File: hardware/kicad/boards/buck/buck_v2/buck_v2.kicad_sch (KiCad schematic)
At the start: 23 parts, among them J1 9V Battery, J2 MCP PWM, J3 Conn_01x02_Socket, Q1 IRF530, SW1 Switch, U1 LM7805, U2 NE555, U3 4N25

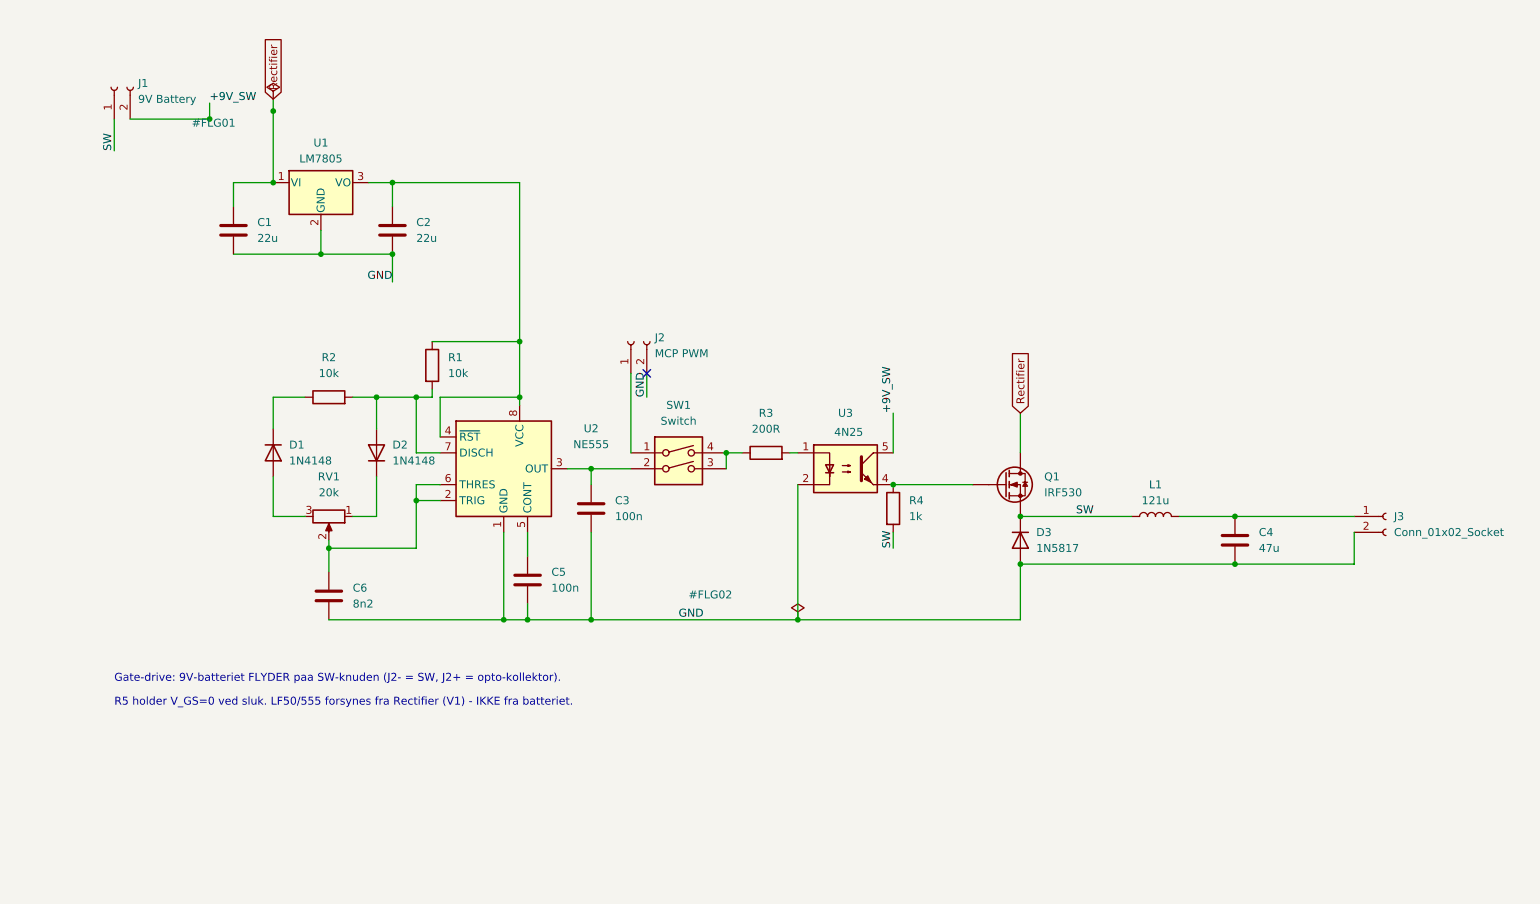
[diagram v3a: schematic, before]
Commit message: Boost v2 med IR2110 gate-driver + boost test-resultater
- boost_v2: integreret IR2110 gate-drive (opto -> IR2110 -> low-side MOSFET),
  generator (build_boost_v2.py), schematic, board og laser/gerber-filer
- buck_v2: patchet til IR2110 high-side drive (patch_buck_v2_ir2110.py)
- boost: opdateret board, gamle produktions-DXF erstattet af boost_v2
- AD3 boost-bringup script (tools/ad3/boost_test.py)
- BOM opdateret med IR2110/CNY17; CNY17- og IRF530-datablade
- rapport: boost maaleresultater (10 kHz, 40%) med figur
- HANDOFF-dokument for buck/boost IR2110-redesign; PCB_RESULTS opdateret
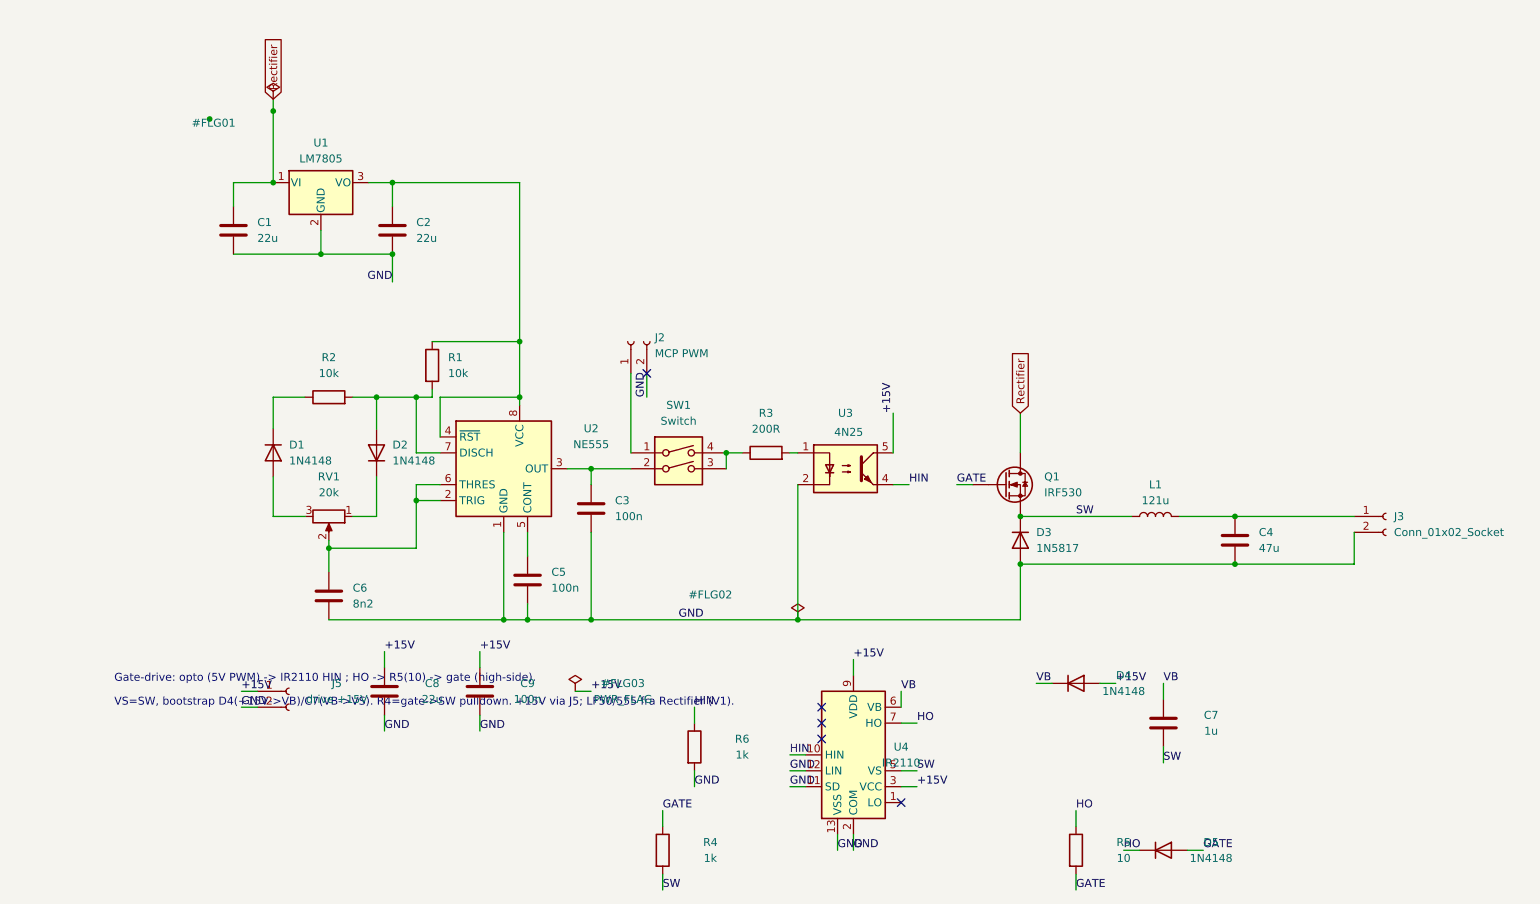
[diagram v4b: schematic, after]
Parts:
- removed J1: 9V Battery, TerminalBlock:TerminalBlock_bornier-2_P5.08mm, symbol Connector:Conn_01x02_Socket
- added C7: 1u, Capacitor_THT:C_Disc_D5.0mm_W2.5mm_P5.00mm, symbol Device:C
- added C8: 22u, Capacitor_THT:CP_Radial_D8.0mm_P3.50mm, symbol Device:C
- added C9: 100n, Capacitor_THT:C_Disc_D5.0mm_W2.5mm_P5.00mm, symbol Device:C
- added D4, D5: 1N4148, Diode_THT:D_DO-35_SOD27_P7.62mm_Horizontal, symbol Device:D
- added J5: drive +15V, TerminalBlock:TerminalBlock_bornier-2_P5.08mm, symbol Connector:Conn_01x02_Socket
- added R5: 10, Resistor_THT:R_Axial_DIN0207_L6.3mm_D2.5mm_P7.62mm_Horizontal, symbol Device:R
- added R6: 1k, Resistor_THT:R_Axial_DIN0207_L6.3mm_D2.5mm_P7.62mm_Horizontal, symbol Device:R
- added U4: IR2110, Package_DIP:DIP-14_W7.62mm_LongPads, symbol Driver_FET:IR2110
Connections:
- net GND: now also C8.2, C9.2, J5.2 (Pin_2), R6.2, U4.11 (SD), U4.12 (LIN), U4.13 (VSS), U4.2 (COM)
- net SW: now also C7.2, U4.5 (VS)
- net GATE: now reaches Q1.G, R4.1
- net GATE: now also D5.2 (A), R5.2; no longer U3.4
- net +9V_SW renamed +15V
- net +15V: now also C8.1, C9.1, D4.2 (A), J5.1 (Pin_1), U4.3 (VCC), U4.9 (VDD)
- new net HIN: R6.1, U3.4, U4.10 (HIN)
- new net HO: D5.1 (K), R5.1, U4.7 (HO)
- new net VB: C7.1, D4.1 (K), U4.6 (VB)
- no-connect marks 1 -> 5
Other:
- note added: "Gate-drive: opto (5V PWM) -> IR2110 HIN ; HO -> R5(10) -> gate (high-side)."
- note added: "VS=SW, bootstrap D4(+15V->VB)/C7(VB->VS). R4=gate->SW pulldown. +15V via J5; LF50/555 fra Rectifier (V1)."
- note removed: "Gate-drive: 9V-batteriet FLYDER paa SW-knuden (J2- = SW, J2+ = opto-kollektor)."
- note removed: "R5 holder V_GS=0 ved sluk. LF50/555 forsynes fra Rectifier (V1) - IKKE fra batteriet."

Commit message: Buck_v2 routet + MPPT-buck board + audit/handoff
- buck_v2: enkeltsidet route faerdig (0 uroutede, 0 vias, 8 traadbroer);
  C6 8n2 box-footprint; faerdige laser-DXF; placerings-SVG matcher boardet
- mppt_buck: ny switching-buck til MPPT (PV ~17.6V -> 5V lager, IR2110
  high-side, Arduino P&O) - board, generator (build_mppt_buck.py), produktion
- BOM/footprint_map + PCB_RESULTS opdateret
- AUDIT (buck/boost IR2110) + HANDOFF (mppt buck) dokumenter
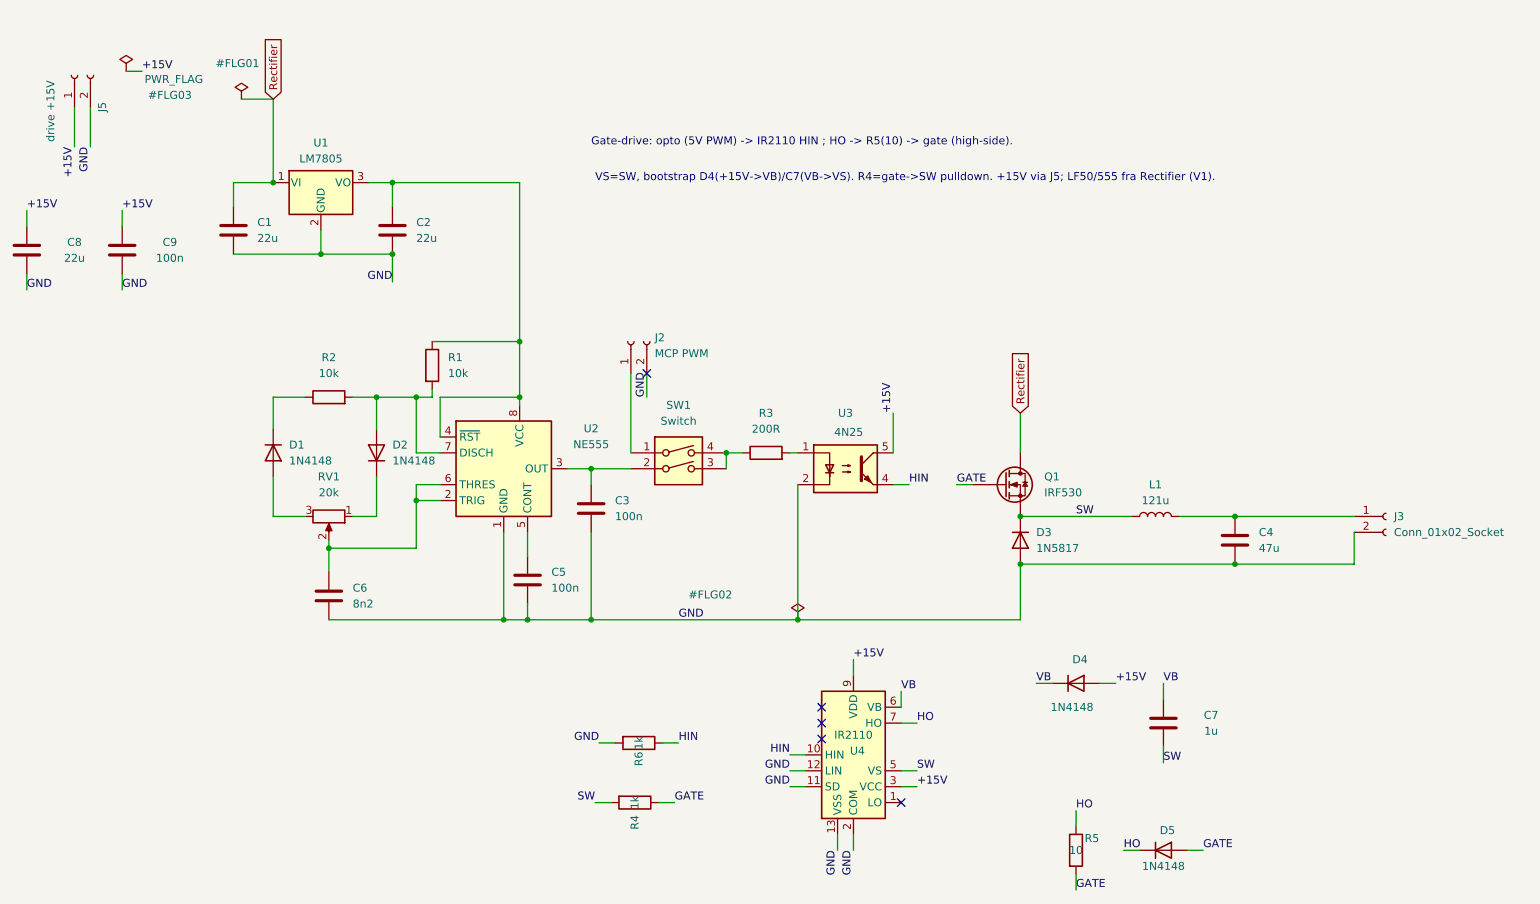
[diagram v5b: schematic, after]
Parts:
- C6: footprint Capacitor_THT:C_Disc_D5.0mm_W2.5mm_P5.00mm -> Capacitor_THT:C_Rect_L13.0mm_W6.0mm_P10.00mm_FKS3_FKP3_MKS4
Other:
- moved on the sheet: C8, C9, J5, R4, R6

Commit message: Assign G/D/S TO-220 footprint to Q_NMOS MOSFETs across boards (match symbol pins)
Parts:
- Q1: footprint energy_system:TO-220-3_Vertical_LaserPads -> energy_system:TO-220-3_Vertical_LaserPads_GDS
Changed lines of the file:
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@@
 			)
 		)
-		(property "Footprint" "energy_system:TO-220-3_Vertical_LaserPads"
+		(property "Footprint" "energy_system:TO-220-3_Vertical_LaserPads_GDS"
 			(at 179.07 83.82 0)
 			(effects

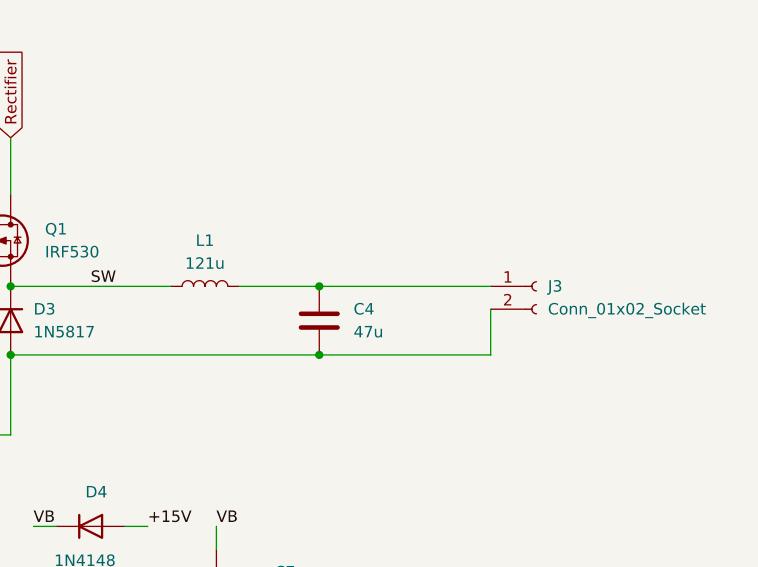
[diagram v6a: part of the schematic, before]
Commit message: system PCB: routing prep (track 1.0, GND pour both layers) + board/CAM updates
system board:
- fix Default netclass track 0.9 -> 1.0 mm (was below min_track_width, every
  trace would have failed DRC); clearance 1.0, via 2.4/1.0 in .kicad_pro + board
- pour GND on F.Cu and B.Cu (edge inset 0.5 mm, solid pad tie)
- routing tooling: route_prep (netclass+pour), export_dsn_noplane (route GND as
  tracks; Freerouting 1.9.0 chokes on full-board planes), route_finish (SES
  import + refill + sparse GND stitching), inspect_system

srm-cam: bump submodule to double-sided support (90 rotation, bottom-side bed
leveling, GUI ruler/STOP/probe-grid, run-time estimator)

production: rename boost_v2_mill nc -> board_*, add drive_circuit trace rework
boards: buck_v2, current_sense, c2000_feedback edits; BOM + AD3 lab-guide
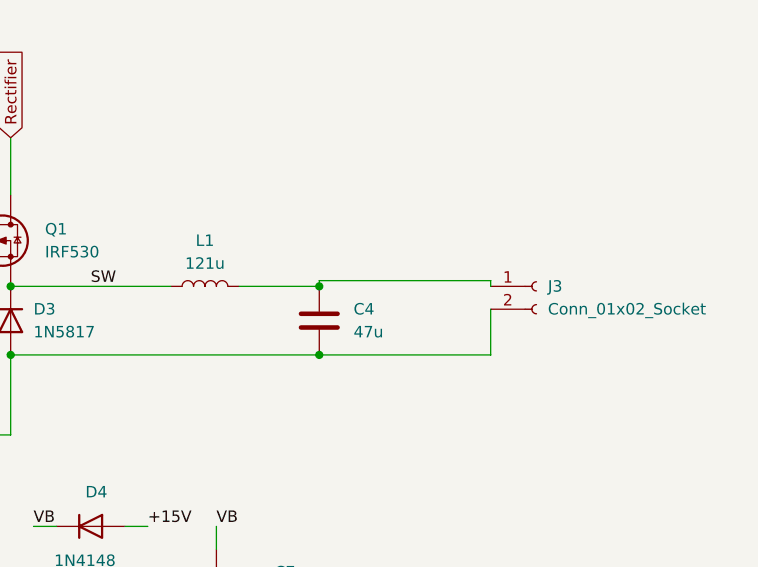
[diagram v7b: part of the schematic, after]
